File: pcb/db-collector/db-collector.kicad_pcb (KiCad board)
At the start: 2 copper layers, 18.3 x 32.1 mm, 18 parts, among them IC1 ICS-43432, IC2 TLV75533PDYDR, J1 Power, U1 XAIO ESP32-C3

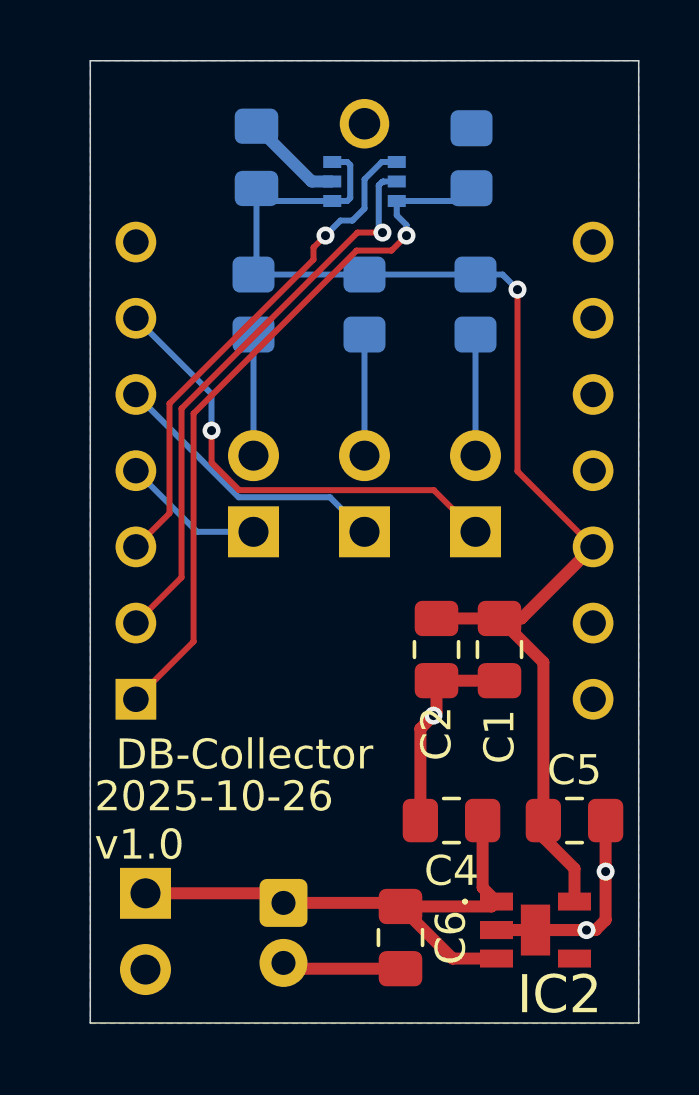
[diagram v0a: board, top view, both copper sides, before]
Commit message: New simplified db-collector.  Big change is that the battery attaches directly to the ESP32-c3 XIAO battery terminals and lets it do the voltage regulation.  This gets around how finicky the ESP is to slow voltage rampup on the 3V3 rail.
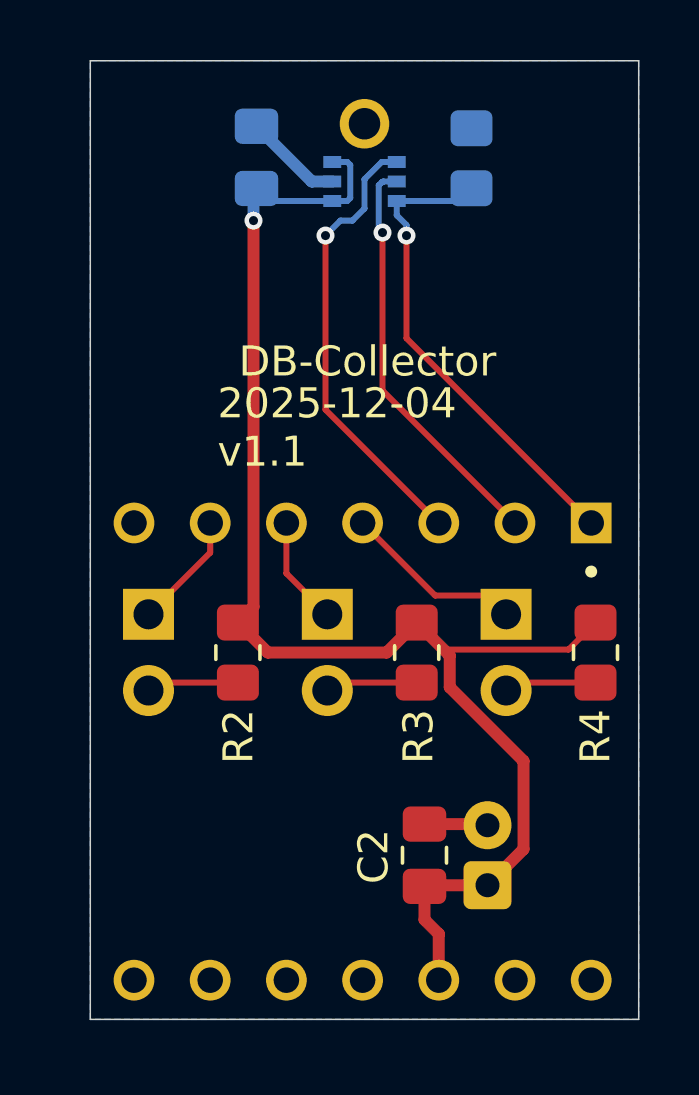
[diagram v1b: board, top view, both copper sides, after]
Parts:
- removed C1: 10uF, Capacitor_SMD:C_0805_2012Metric_Pad1.18x1.45mm_HandSolder
- removed C4, C5: 1uF, Capacitor_SMD:C_0805_2012Metric_Pad1.18x1.45mm_HandSolder
- removed C6: .1uF, Capacitor_SMD:C_0805_2012Metric_Pad1.18x1.45mm_HandSolder
- removed IC2: TLV75533PDYDR, Garth:TLV75533PDYDR
- removed J1: Power, Connector_PinHeader_2.54mm:PinHeader_1x02_P2.54mm_Vertical
- R2, R3, R4, U1: moved to F.Cu
- moved R4 16.3 mm to (147.5, 82.4)
- moved R2 14.0 mm to (135.6, 82.4)
- moved R3 11.7 mm to (141.5, 82.4)
- moved D3 11.2 mm to (132.6, 81.1), turned to 180 degrees
- moved U1 9.30 mm to (139.8, 85.7), turned to -90 degrees
- moved D1 8.86 mm to (144.5, 81.1), turned to 180 degrees
- moved C2 6.87 mm to (141.8, 89.2), turned to 90 degrees
- moved C10 6.83 mm to (143.9, 90.2), turned to 90 degrees
- moved D2 3.02 mm to (138.6, 81.1), turned to 180 degrees
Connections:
- C10 pad 1: +BATT -> +3.3V
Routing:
- net +BATT: track 18.9 -> 0.00 mm
- net GND: track 21.3 -> 5.40 mm, vias 3 -> 0
- net Net-(D3-K): track 15.6 -> 3.90 mm, vias 1 -> 0
- net /SD: track 23.8 -> 16.1 mm
- net +3.3V: track 43.3 -> 49.5 mm
- net Net-(D2-K): track 9.52 -> 3.61 mm
- net /SCK: track 19.2 -> 13.8 mm
- net /WS: track 17.0 -> 15.1 mm
- net Net-(D1-K): track 4.76 -> 6.04 mm
- net Net-(D2-A): track 4.03 -> 3.09 mm
- net Net-(D1-A): track 4.03 -> 3.09 mm
- net Net-(D3-A): track 4.03 -> 3.09 mm
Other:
- board size 18.3 x 32.1 mm -> 18.3 x 32 mm
- board text added: "2025-12-04 v1.1"
- board text added: "[BOARD_COST] 0.722in x 1.260in | 0.909 in^2 | $4.55"
- board text removed: "2025-10-26 v1.0"
- board text removed: "BATT"
- board text removed: "[BOARD_COST] 0.722in x 1.024in | 0.739 in^2 | $3.69"
